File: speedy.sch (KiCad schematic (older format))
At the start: 40 parts, among them U1 STM32F415RGT6, U2 NUF2042VX6, X1 16Mhz 10ppm

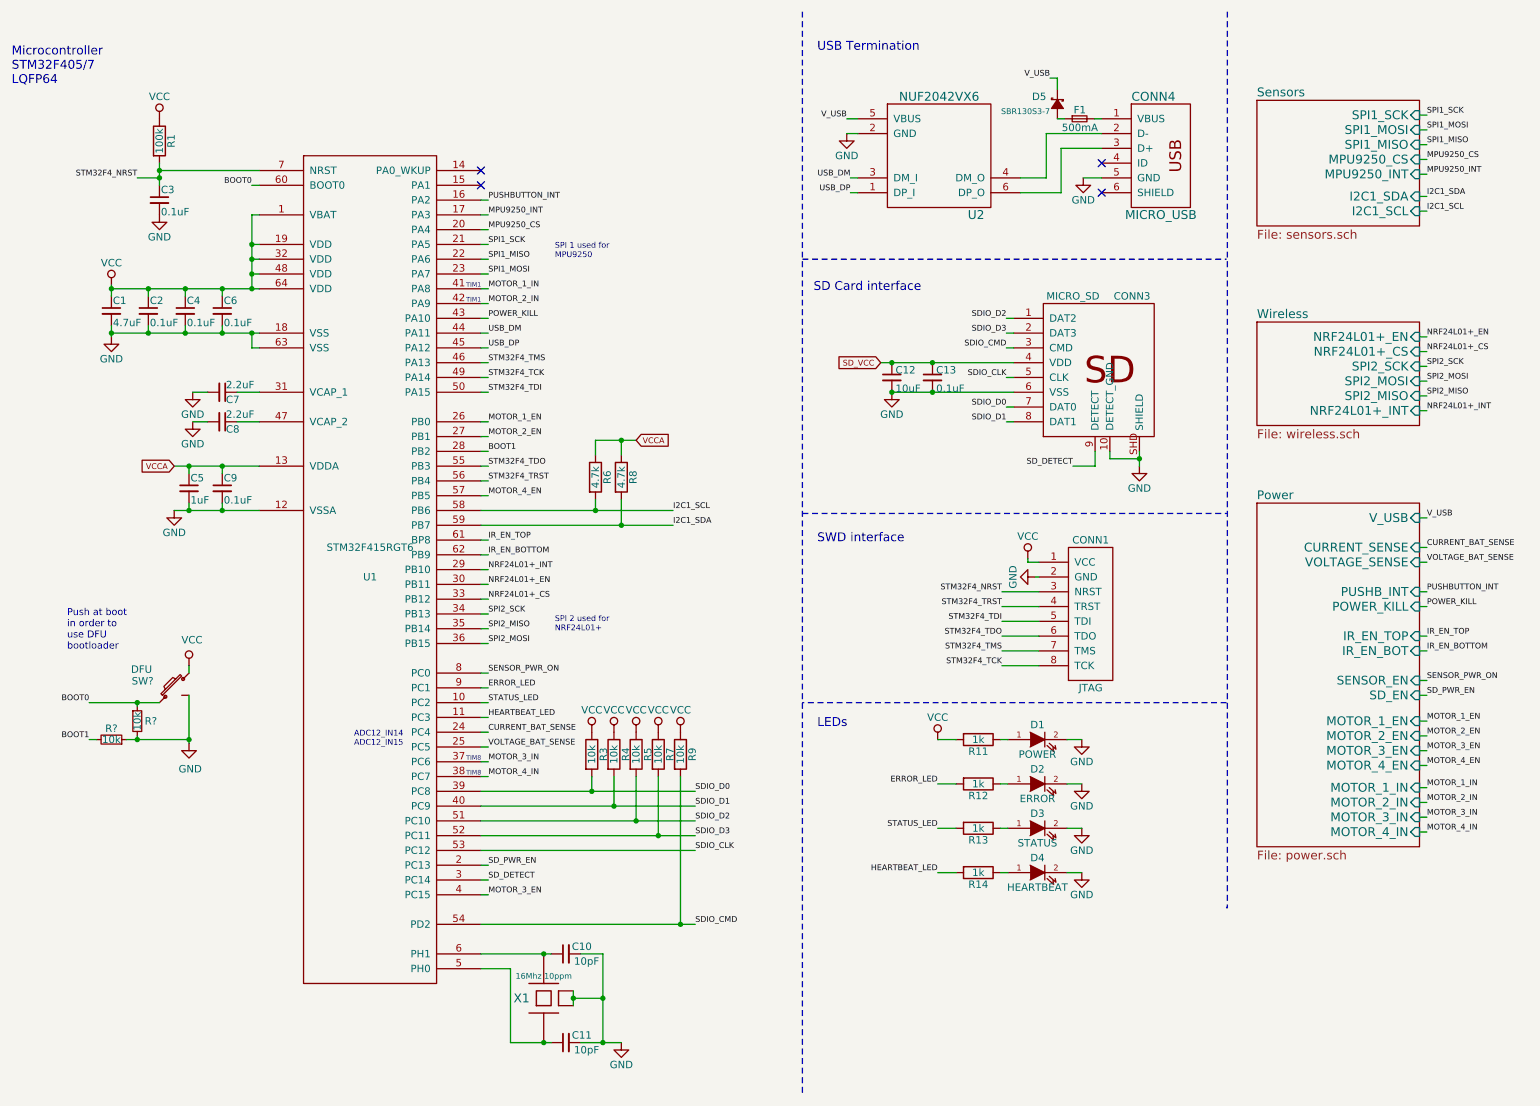
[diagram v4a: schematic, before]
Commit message: Fix problems noted by @nuft during review
- Force pulldown on unused bootloadr pins (USART 1 & 3)
- Use one oscillator for both MCU and NRF
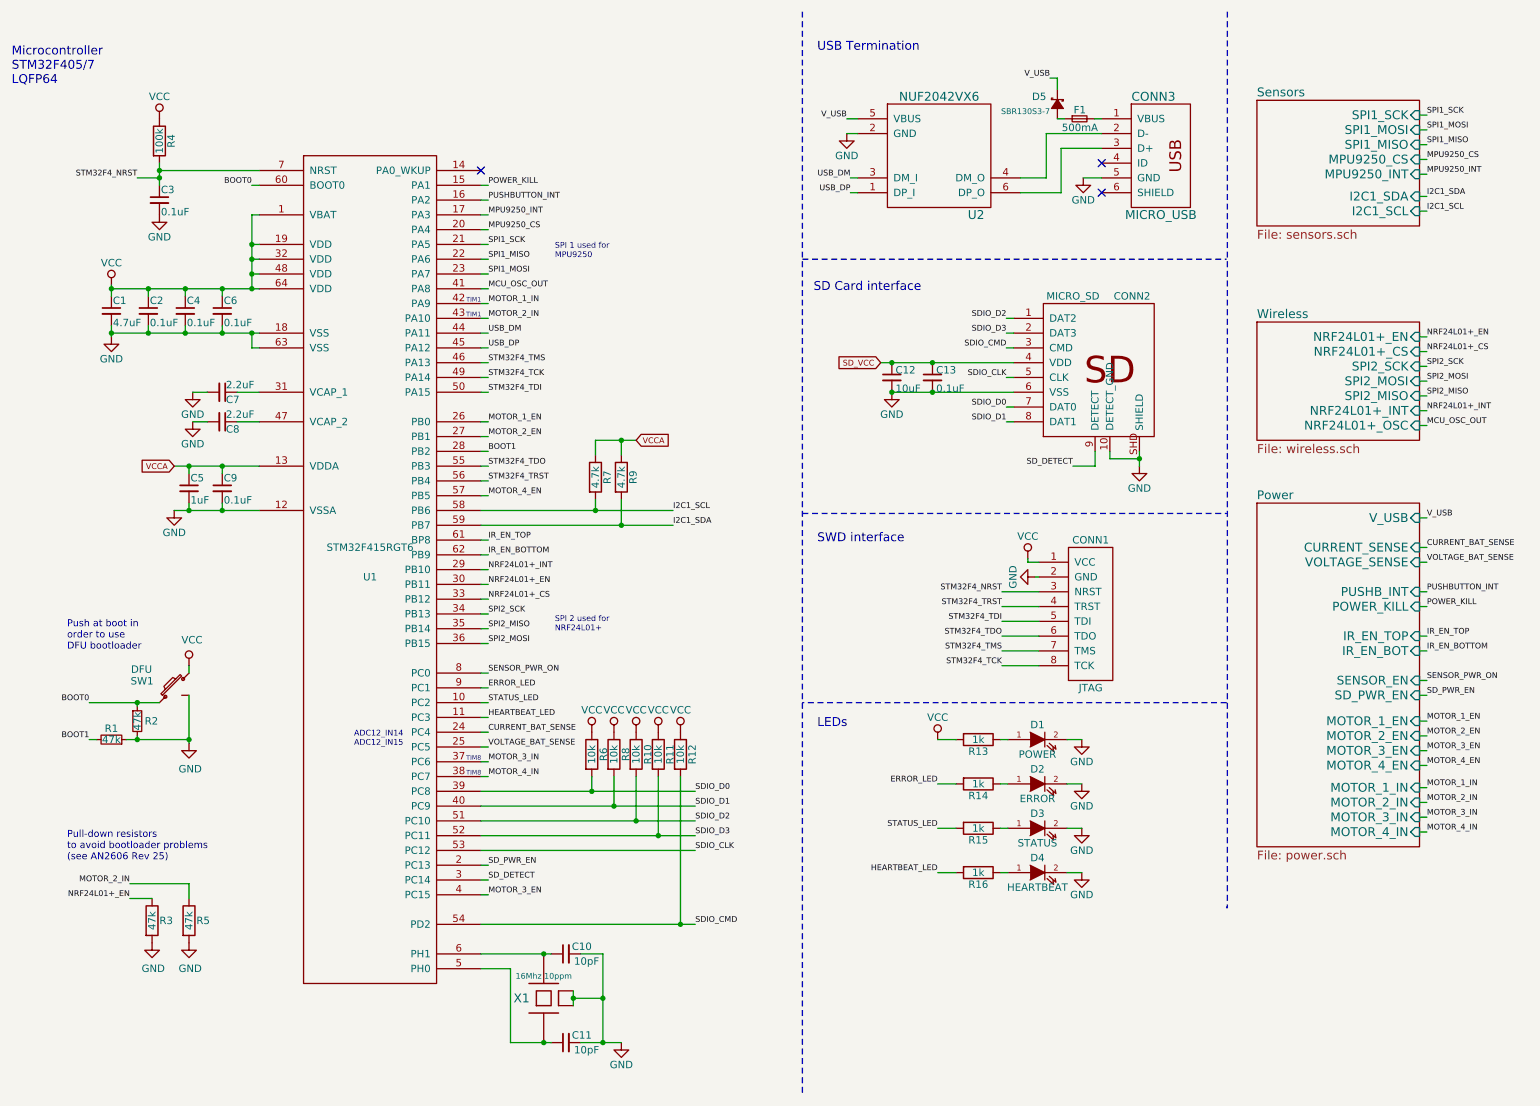
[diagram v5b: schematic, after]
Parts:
- added R3, R5: 47k, _std:_0402, symbol R
- R1, R2: renamed from R?; value 10k -> 47k
- gave numbers to parts that had none: 1
- renumbered CONN3 to CONN2, CONN4 to CONN3, R5 to R10, R7 to R11, R9 to R12, R11 to R13, R12 to R14, R13 to R15, R14 to R16, R1 to R4, R3 to R6, R6 to R7, R4 to R8, R8 to R9
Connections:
- net GND: now also R3.2, R5.2
- net MOTOR_1_IN: now also U1.42 (PA9); no longer U1.41 (PA8)
- net MOTOR_2_IN: now also U1.43 (PA10), R5.1; no longer U1.42 (PA9)
- net NRF24L01+_EN: now also R3.1
- net POWER_KILL: now also U1.15 (PA1); no longer U1.43 (PA10)
- new net MCU_OSC_OUT: U1.41 (PA8)
- no-connect marks 4 -> 3
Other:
- note added: "Pull-down resistors \nto avoid bootloader problems \n(see AN2606 Rev 25)"
- note added: "Push at boot in \norder to use \nDFU bootloader"
- note removed: "Push at boot \nin order to\nuse DFU \nbootloader"

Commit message: (Re)Place components on PCB
Netlist was broken after review corrections
Rebuilt and placed components from scratch
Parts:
- R1, R2: footprint (none) -> _std:_0402
- SW1: footprint (none) -> _div:SMD_Pushbutton_B3U-3100P
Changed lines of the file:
@@
 F 0 "SW1" V 1796 5190 50  0000 L CNN
 F 1 "DFU" V 1875 5200 50  0000 L CNN
-F 2 "" H 1750 5050 50  0000 C CNN
+F 2 "_div:SMD_Pushbutton_B3U-3100P" H 1750 5050 50  0001 C CNN
 F 3 "" H 1750 5050 50  0000 C CNN
 	1    1750 5050
@@
 F 0 "R2" H 1550 5275 50  0000 L CNN
 F 1 "47k" V 1500 5275 50  0000 C CNN
-F 2 "" H 1500 5275 50  0000 C CNN
+F 2 "_std:_0402" H 1500 5275 50  0001 C CNN
 F 3 "" H 1500 5275 50  0000 C CNN
 	1    1500 5275
@@
 F 0 "R1" V 1400 5400 50  0000 C CNN
 F 1 "47k" V 1325 5400 50  0000 C CNN
-F 2 "" H 1325 5400 50  0000 C CNN
+F 2 "_std:_0402" H 1325 5400 50  0001 C CNN
 F 3 "" H 1325 5400 50  0000 C CNN
 	1    1325 5400

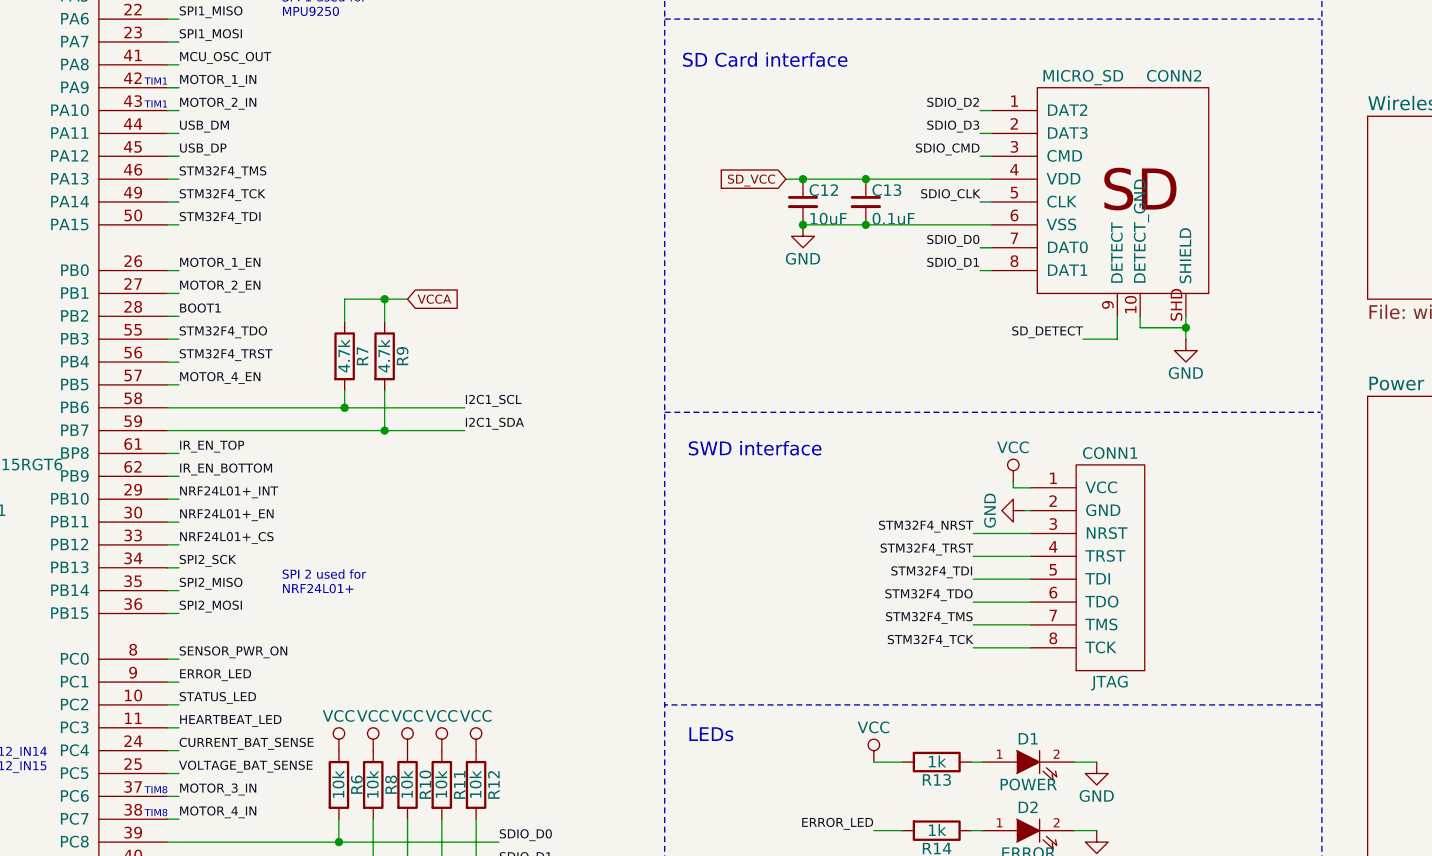
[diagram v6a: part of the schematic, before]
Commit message: Update debug connector to use new CVRA convention
SWD + UART connector using Molex picoblade 7pin connector
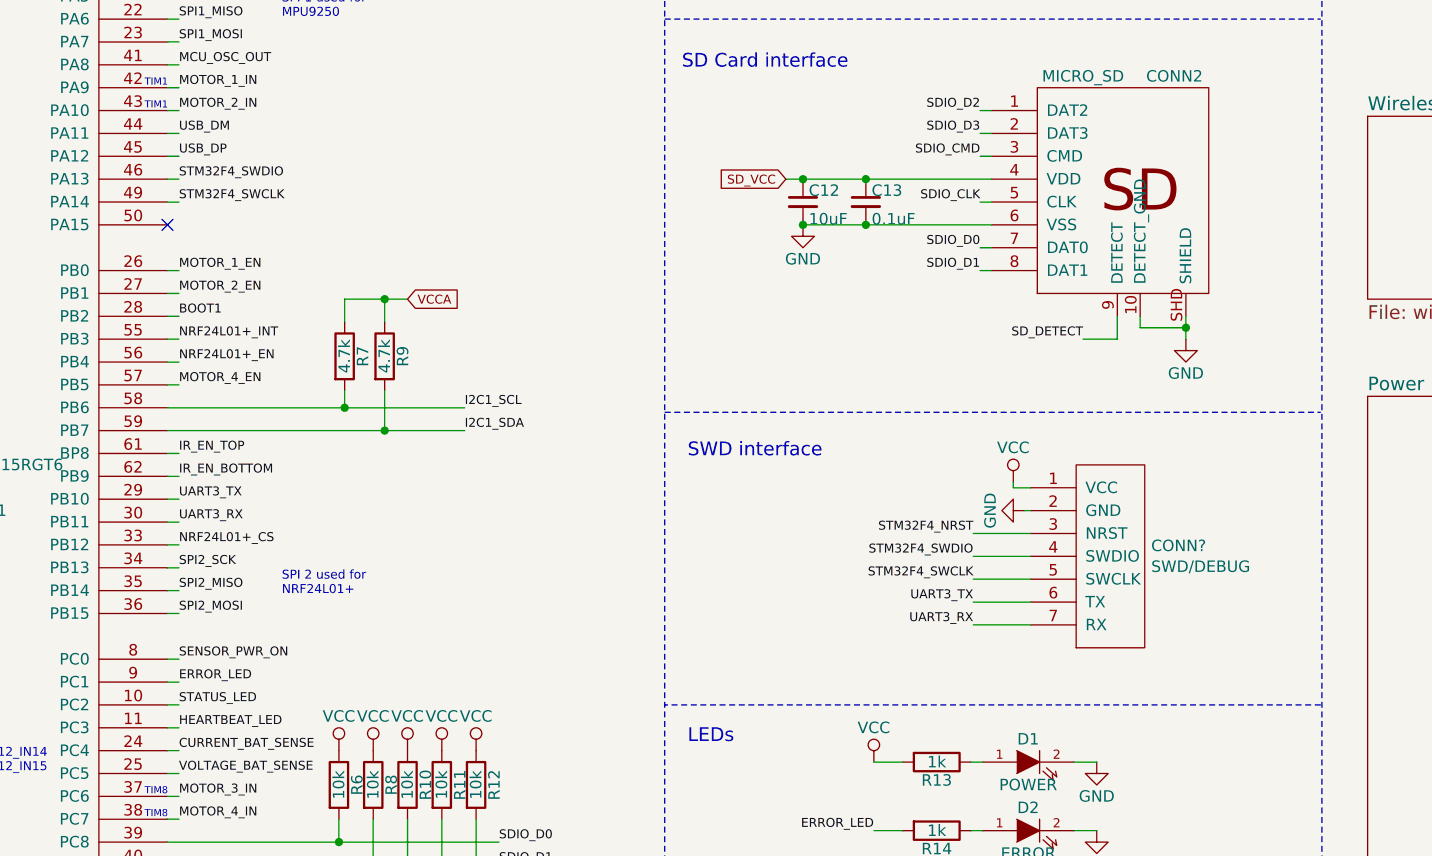
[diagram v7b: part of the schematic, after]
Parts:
- removed CONN1: JTAG, _connectors:_Molex-PicoBlade-SMD-8, symbol JTAG
- added CONN?: SWD/DEBUG, MODULE, symbol SWD/DEBUG
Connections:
- net STM32F4_TDO is gone; now on net NRF24L01+_INT: U1.55 (PB3)
- net STM32F4_TRST is gone; now on net NRF24L01+_EN: U1.56 (PB4)
- net GND: now also CONN?.2 (GND), CONN?.MECH (GND)
- net NRF24L01+_EN: no longer U1.30 (PB11)
- net NRF24L01+_INT: no longer U1.29 (PB10)
- net STM32F4_NRST: now also CONN?.3 (NRST)
- net VCC: now also CONN?.1 (VCC)
- net STM32F4_TCK renamed STM32F4_SWCLK
- net STM32F4_SWCLK: now also CONN?.5 (SWCLK)
- net STM32F4_TDI: no longer names the net of U1.50 (PA15)
- net STM32F4_TMS renamed STM32F4_SWDIO
- net STM32F4_SWDIO: now also CONN?.4 (SWDIO)
- new net UART3_RX: CONN?.7 (RX), U1.30 (PB11)
- new net UART3_TX: CONN?.6 (TX), U1.29 (PB10)
- no-connect marks 3 -> 4
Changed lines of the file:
@@
 Text Label 3875 4750 0    39   ~ 0
 SPI2_MOSI
-Text Label 3875 4350 0    39   ~ 0
+Text Label 3875 3650 0    39   ~ 0
 NRF24L01+_EN
-Text Label 3875 4250 0    39   ~ 0
+Text Label 3875 3550 0    39   ~ 0
 NRF24L01+_INT
 Text Notes 4325 4675 0    39   ~ 0
@@
 Text Label 7350 4400 2    39   ~ 0
 STM32F4_NRST
-Text Label 3875 2850 0    39   ~ 0
-STM32F4_TMS
-Text Label 3875 2950 0    39   ~ 0
-STM32F4_TCK
 $Comp
 L LED-RESCUE-speedy D1
@@
 Text Label 3875 6250 0    39   ~ 0
 SD_PWR_EN
-Text Label 3875 3550 0    39   ~ 0
-STM32F4_TDO
-Text Label 3875 3650 0    39   ~ 0
-STM32F4_TRST
-Text Label 7350 4700 2    39   ~ 0
-STM32F4_TDO
-Text Label 7350 4500 2    39   ~ 0
-STM32F4_TRST
-Text Label 3875 3050 0    39   ~ 0
-STM32F4_TDI
-Text Label 7350 4600 2    39   ~ 0
-STM32F4_TDI
-Text Label 7350 4900 2    39   ~ 0
-STM32F4_TCK
-Text Label 7350 4800 2    39   ~ 0
-STM32F4_TMS
-$Comp
-L JTAG CONN1
-U 1 1 55C96701
-P 7950 4550
-F 0 "CONN1" H 7950 5050 50  0000 C CNN
-F 1 "JTAG" H 7950 4050 50  0000 C CNN
-F 2 "_connectors:_Molex-PicoBlade-SMD-8" H 7950 4550 50  0001 C CNN
-F 3 "DOCUMENTATION" H 7950 4550 50  0001 C CNN
-	1    7950 4550
-	1    0    0    -1
-$EndComp
 $Comp
 L GND #PWR022
@@
 	7350 4800 7600 4800
 Wire Wire Line
-	7350 4900 7600 4900
-Wire Wire Line
 	7600 4600 7350 4600
 Wire Wire Line
@@
 Wire Wire Line
 	7350 4400 7600 4400
-Wire Wire Line
-	3875 3650 3825 3650
-Wire Wire Line
-	3875 3550 3825 3550
 Wire Notes Line
 	6000 2150 8870 2150
@@
 	3875 4250 3825 4250
 Wire Wire Line
-	3825 3050 3875 3050
-Wire Wire Line
 	3825 2750 3875 2750
 Wire Wire Line
@@
 Text Notes 1025 6225 0    47   ~ 0
 Pull-down resistors \nto avoid bootloader problems \n(see AN2606 Rev 25)
+$Comp
+L SWD/DEBUG CONN?
+U 1 1 57531C38
+P 7950 4500
+F 0 "CONN?" H 8128 4546 50  0000 L CNN
+F 1 "SWD/DEBUG" H 8128 4455 50  0000 L CNN
+F 2 "MODULE" H 7950 4450 50  0001 C CNN
+F 3 "DOCUMENTATION" H 7950 4450 50  0001 C CNN
+	1    7950 4500
+	1    0    0    -1
+$EndComp
+Text Label 3875 2850 0    39   ~ 0
+STM32F4_SWDIO
+Text Label 3875 2950 0    39   ~ 0
+STM32F4_SWCLK
+NoConn ~ 3825 3050
+Wire Wire Line
+	3875 3550 3825 3550
+Wire Wire Line
+	3875 3650 3825 3650
+Text Label 3875 4250 0    39   ~ 0
+UART3_TX
+Text Label 3875 4350 0    39   ~ 0
+UART3_RX
+Text Label 7350 4800 2    39   ~ 0
+UART3_RX
+Text Label 7350 4700 2    39   ~ 0
+UART3_TX
+Text Label 7350 4600 2    39   ~ 0
+STM32F4_SWCLK
+Text Label 7350 4500 2    39   ~ 0
+STM32F4_SWDIO
 $EndSCHEMATC
